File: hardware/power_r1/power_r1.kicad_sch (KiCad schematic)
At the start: 25 parts, among them J101 PWR_IN, J102 PWR_OUT_P

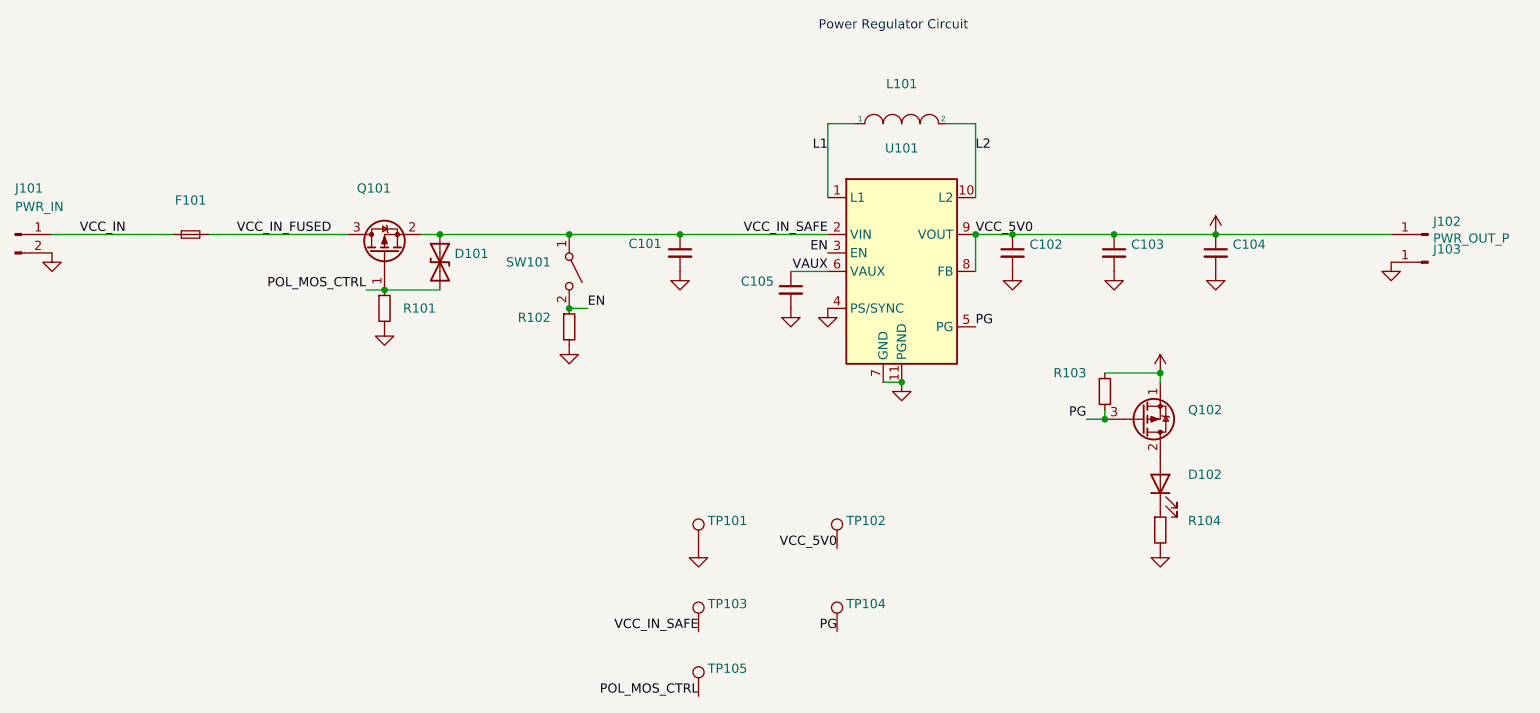
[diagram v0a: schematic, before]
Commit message: Display board layout is now 95% complete, the number of caps on the board might need some further tweaking and there are also some gaps where a few more LEDs could fit. Additionally I've decided to provide the option to use the hinges as the ground connection allowing more +5V channels on the FFC connectors which should mean more current carrying capacity. The new power board schematic has had some changes, namely the vreg has changed and so have some of the passives around it, more input protect has been added, a MOV for over voltage protection and an NMOS for reverse pol. Looking at the new vreg the power dissipation before it cooks itself (~1.1W) isn't great but it's enough for about 2.5A (at around 93% eff.) for the LEDs which hasn't usually been the bottleneck (looking at you 9V batteries). This means we're expecting around 1.8A peak input current at a Vin of 7V and need to size the fuze around that as much more current and the vreg is cooked. Might look into a over voltage shutout circuit if it seems like we're blowing fuses too often.
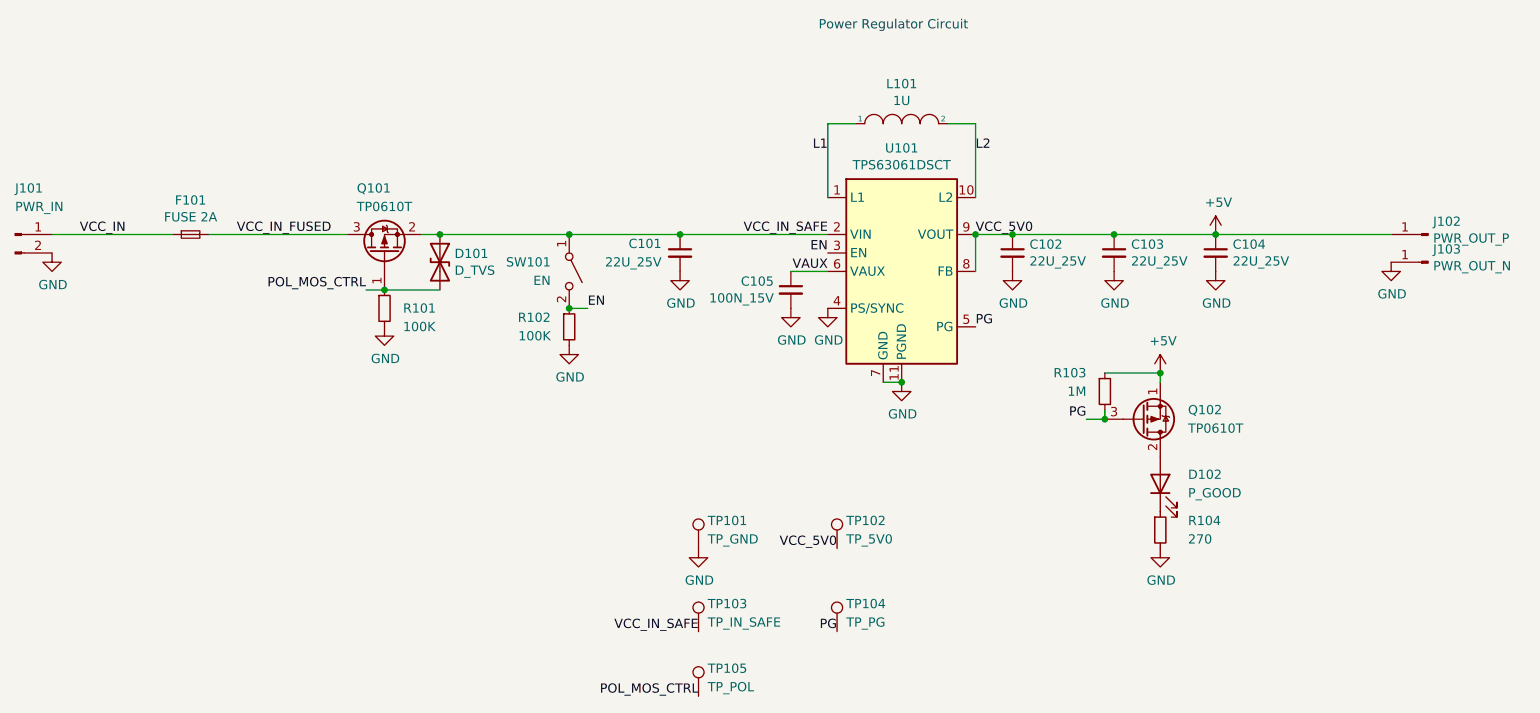
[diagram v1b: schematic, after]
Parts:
- C101, C102, C103, C104: value (none) -> 22U_25V; footprint (none) -> Capacitor_SMD:C_0805_2012Metric
- C105: value (none) -> 100N_15V; footprint (none) -> Capacitor_SMD:C_0805_2012Metric
- D101: value (none) -> D_TVS; footprint (none) -> Diode_SMD:D_SOD-323
- D102: value (none) -> P_GOOD; footprint (none) -> LED_SMD:LED_0805_2012Metric
- F101: value (none) -> FUSE 2A; footprint (none) -> Resistor_SMD:R_1206_3216Metric
- J103: value (none) -> PWR_OUT_N; footprint (none) -> Connector_PinHeader_1.00mm:PinHeader_1x01_P1.00mm_Vertical_SMD_CUSTOM
- L101: value (none) -> 1U; footprint (none) -> Inductor_SMD:L_Taiyo-Yuden_NR-50xx_HandSoldering
- Q101, Q102: value (none) -> TP0610T; footprint (none) -> Package_TO_SOT_SMD:SOT-23
- R101, R102: value (none) -> 100K; footprint (none) -> Resistor_SMD:R_0805_2012Metric
- R103: value (none) -> 1M; footprint (none) -> Resistor_SMD:R_0805_2012Metric
- R104: value (none) -> 270; footprint (none) -> Resistor_SMD:R_0805_2012Metric
- SW101: value (none) -> EN; footprint (none) -> digikey-footprints:Switch_Slide_JS202011SCQN
- TP101: value (none) -> TP_GND; footprint (none) -> TestPoint:TestPoint_Pad_D1.0mm
- TP102: value (none) -> TP_5V0; footprint (none) -> TestPoint:TestPoint_Pad_D1.0mm
- TP103: value (none) -> TP_IN_SAFE; footprint (none) -> TestPoint:TestPoint_Pad_D1.0mm
- TP104: value (none) -> TP_PG; footprint (none) -> TestPoint:TestPoint_Pad_D1.0mm
- TP105: value (none) -> TP_POL; footprint (none) -> TestPoint:TestPoint_Pad_D1.0mm
- U101: value (none) -> TPS63061DSCT; footprint (none) -> Package_SON:Texas_S-PWSON-N10

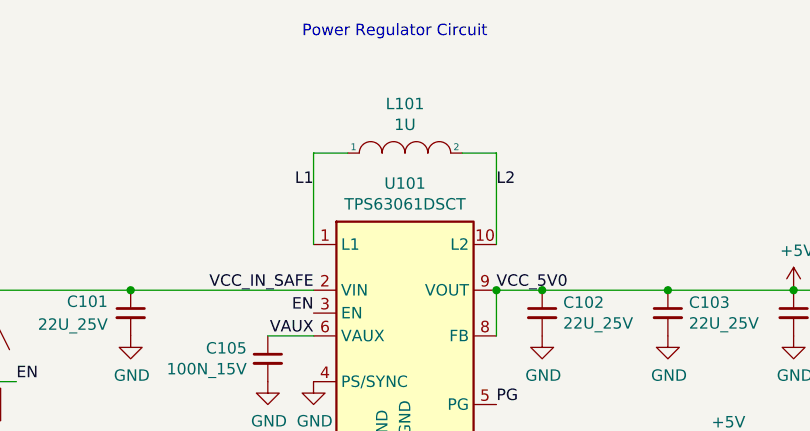
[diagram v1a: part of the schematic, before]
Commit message: Updated kicad files to work with latest kicad. Added some todos for next hw design.
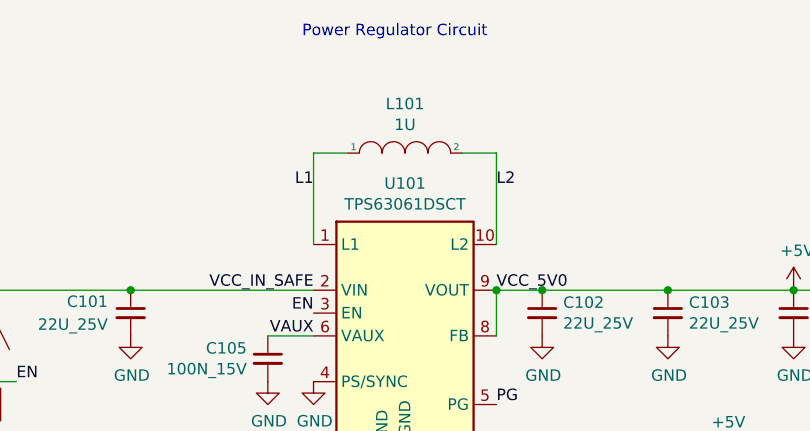
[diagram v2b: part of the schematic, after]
